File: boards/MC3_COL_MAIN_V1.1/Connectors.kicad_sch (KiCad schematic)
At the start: 11 parts, among them J13 HARNESS_FFC_6P, J3 ENC_leaf2, J4 ENC_leaf1, J5 ENC_leaf4, J6 ENC_leaf3

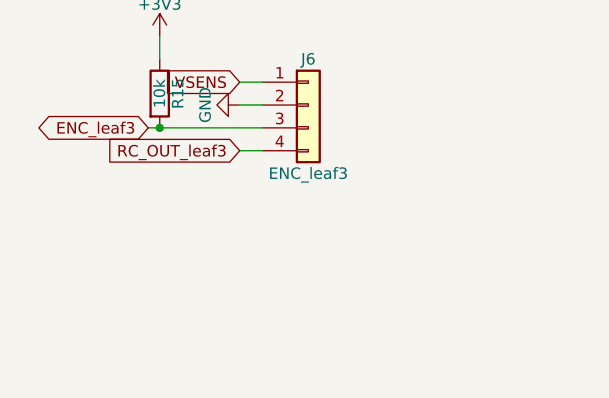
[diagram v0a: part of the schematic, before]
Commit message: V1.1 pre-order (replayed on refactored sheets): ENC_leaf2<->RC_OUT_leaf4 swapped PA3/PA2 (PA3 is TT, PP SENT unsafe); J14 fifth encoder FFC + R48 = YAW_ABS on PA10 (FT); ioc updated; ERC 0/0
Co-Authored-By: Claude Fable 5 <noreply@anthropic.com>
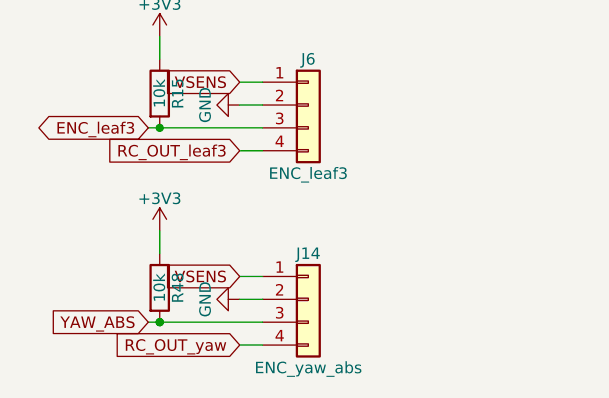
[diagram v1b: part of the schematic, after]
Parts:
- added J14: ENC_yaw_abs, MC3_COL_MAIN:Panasonic_AYF530435_FFC-4P_P0.5mm, symbol Connector_Generic:Conn_01x04
- added R48: 10k, MC3_COL_MAIN:R_0402_1005Metric, symbol Device:R
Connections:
- net +3V3: now also R48.1
- net GND: now also J14.2 (Pin_2)
- net VSENS: now also J14.1 (Pin_1)
- new net RC_OUT_yaw: J14.4 (Pin_4)
- new net YAW_ABS: J14.3 (Pin_3), R48.2
